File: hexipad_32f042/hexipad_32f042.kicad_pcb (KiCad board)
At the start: 2 copper layers, 72 x 62 mm, 36 parts, among them J1 PGM, J10 MNT, J11 MNT, J12 MNT, J13 MNT, J14 ARTWORK, J15 ARTWORK, J16 ARTWORK, J2 USB_B_Micro, J3 PORTB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

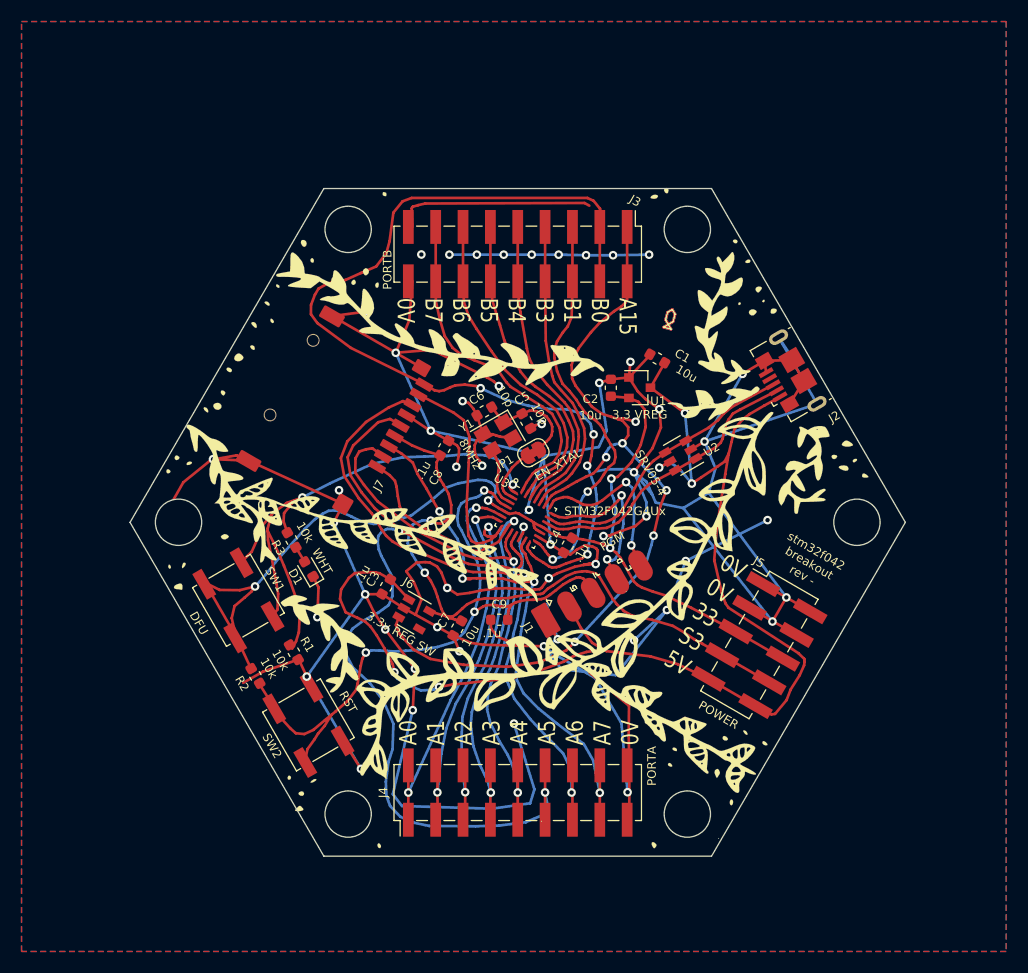
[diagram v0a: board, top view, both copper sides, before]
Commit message: bump revision and rename our breakout to hexipad.
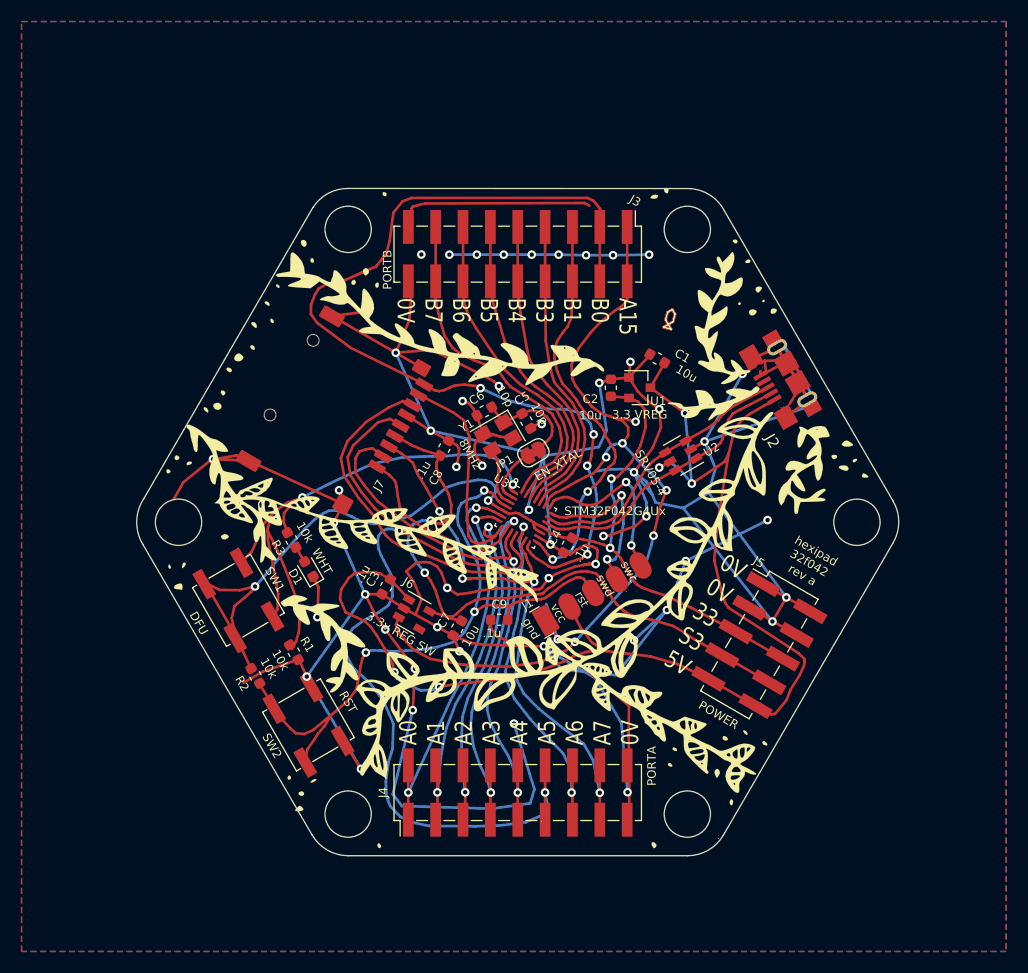
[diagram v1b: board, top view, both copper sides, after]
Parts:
- J1: footprint POGO-5:POGO-5 -> stlink-pgmhdr:POGO-5
- J2: footprint Connector_USB:USB_Micro-B_GCT_USB3076-30-A -> chinese_connectors:chinausb-multi
- moved J2 0.62 mm to (193.5, 58.1), turned to 300 degrees
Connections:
- J6 pad 4: Net-(J6-Pad4) -> (no net)
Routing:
- net GND: track 495.1 -> 517.3 mm
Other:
- board size 72 x 62 mm -> 70.8 x 62 mm
- board text added: "hexipad 32f042 rev a"
- board text removed: "stm32f042 breakout rev -"

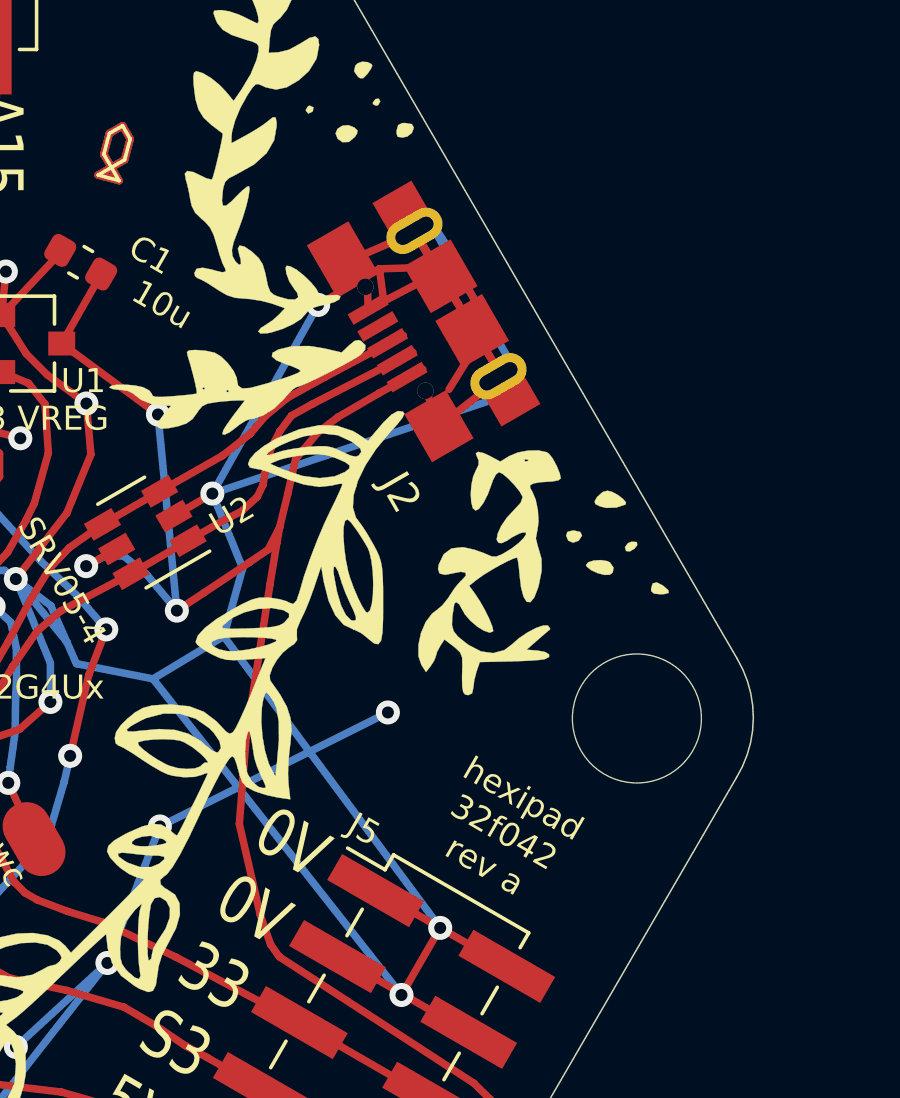
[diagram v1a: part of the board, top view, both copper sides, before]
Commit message: add rev B - fix USB
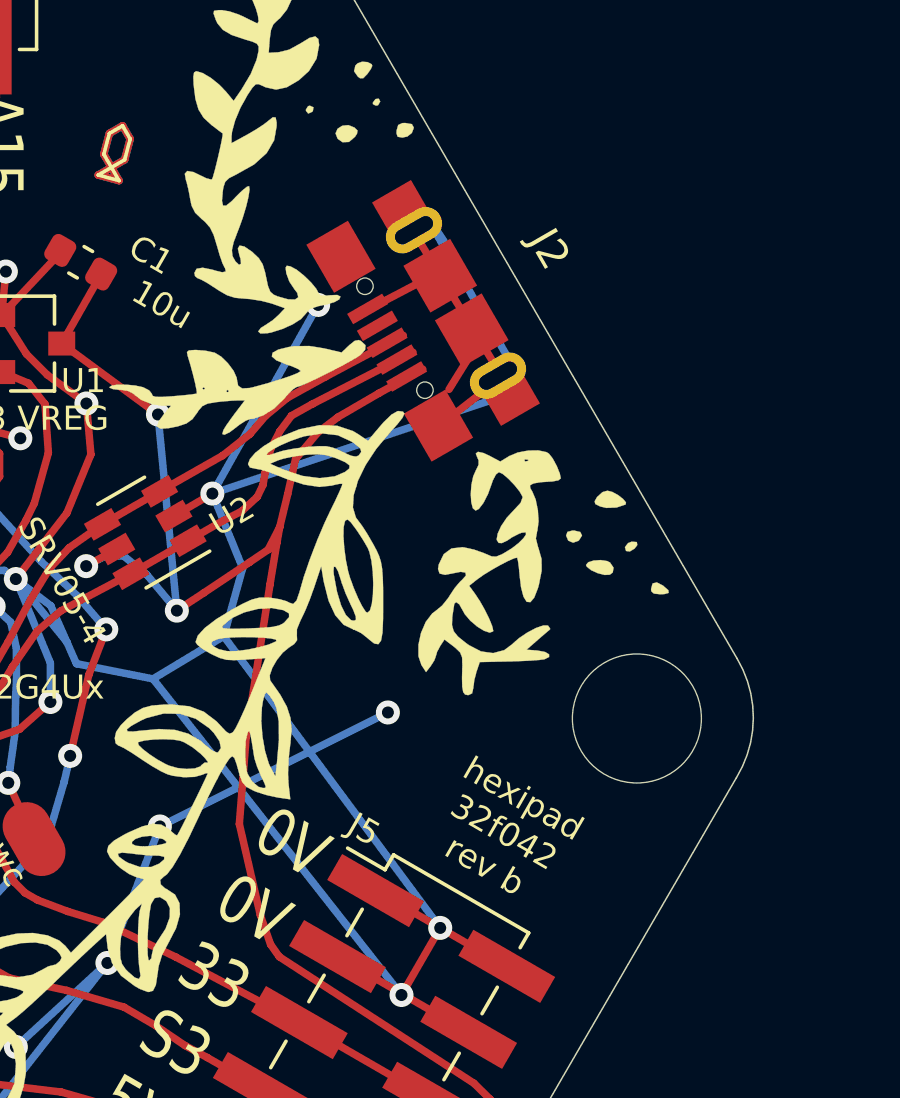
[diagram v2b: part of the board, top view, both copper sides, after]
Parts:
- J2: footprint chinese_connectors:chinausb-multi -> chinese-connectors:chinausb-multi
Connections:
- J6 pad 4: (no net) -> Net-(J6-Pad4)
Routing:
- net GND: track 517.3 -> 497.6 mm
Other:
- board text added: "hexipad 32f042 rev b"
- board text removed: "hexipad 32f042 rev a"
